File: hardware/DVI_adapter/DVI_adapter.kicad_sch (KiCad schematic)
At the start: 49 parts, among them J1 DF12NB(3.0)-30DS-0.5V(51), J2 DF12NB(3.0)-30DS-0.5V(51), J3 FPC Cable connector 1x20, U2 TFP410, U2 TXS0102DQMR

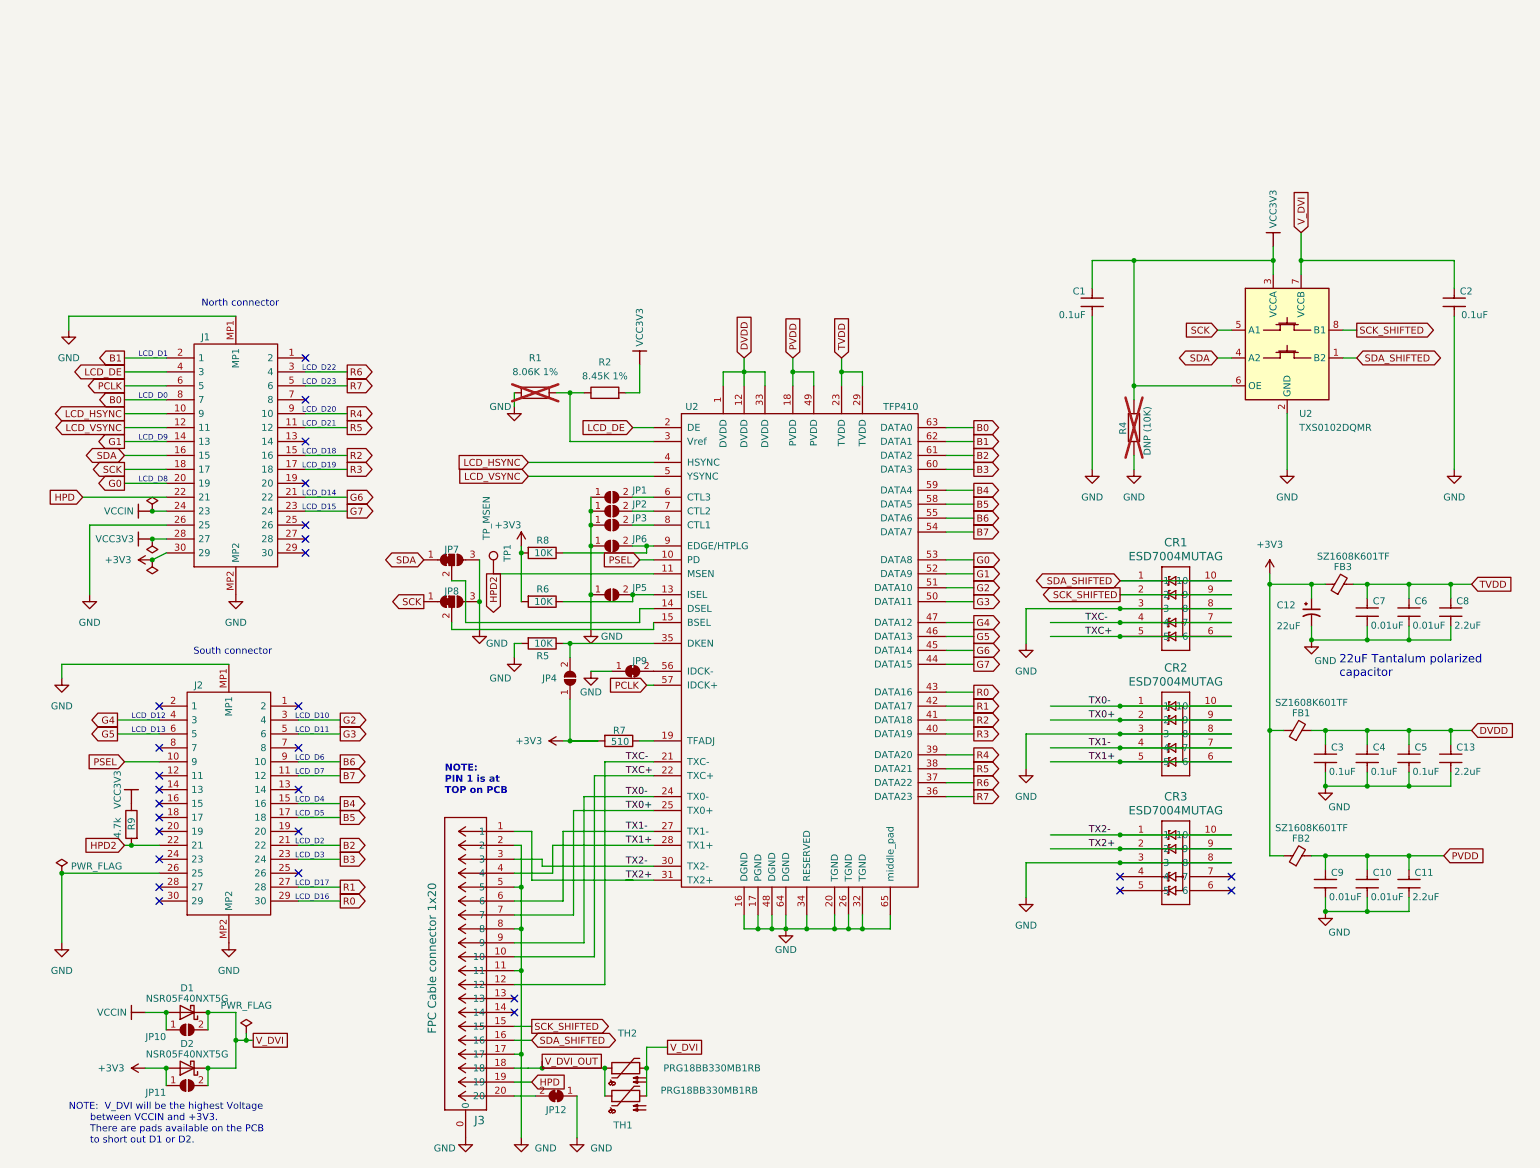
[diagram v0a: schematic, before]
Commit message: Change to 4 layers for better signal integrity. Reorganize differential pins in SSG format to minimize crosstalk at output connector (pinout compatible with common extension cables). Fix level translator footpriont. Add power plane, test points, 5V charge pump, auto reset
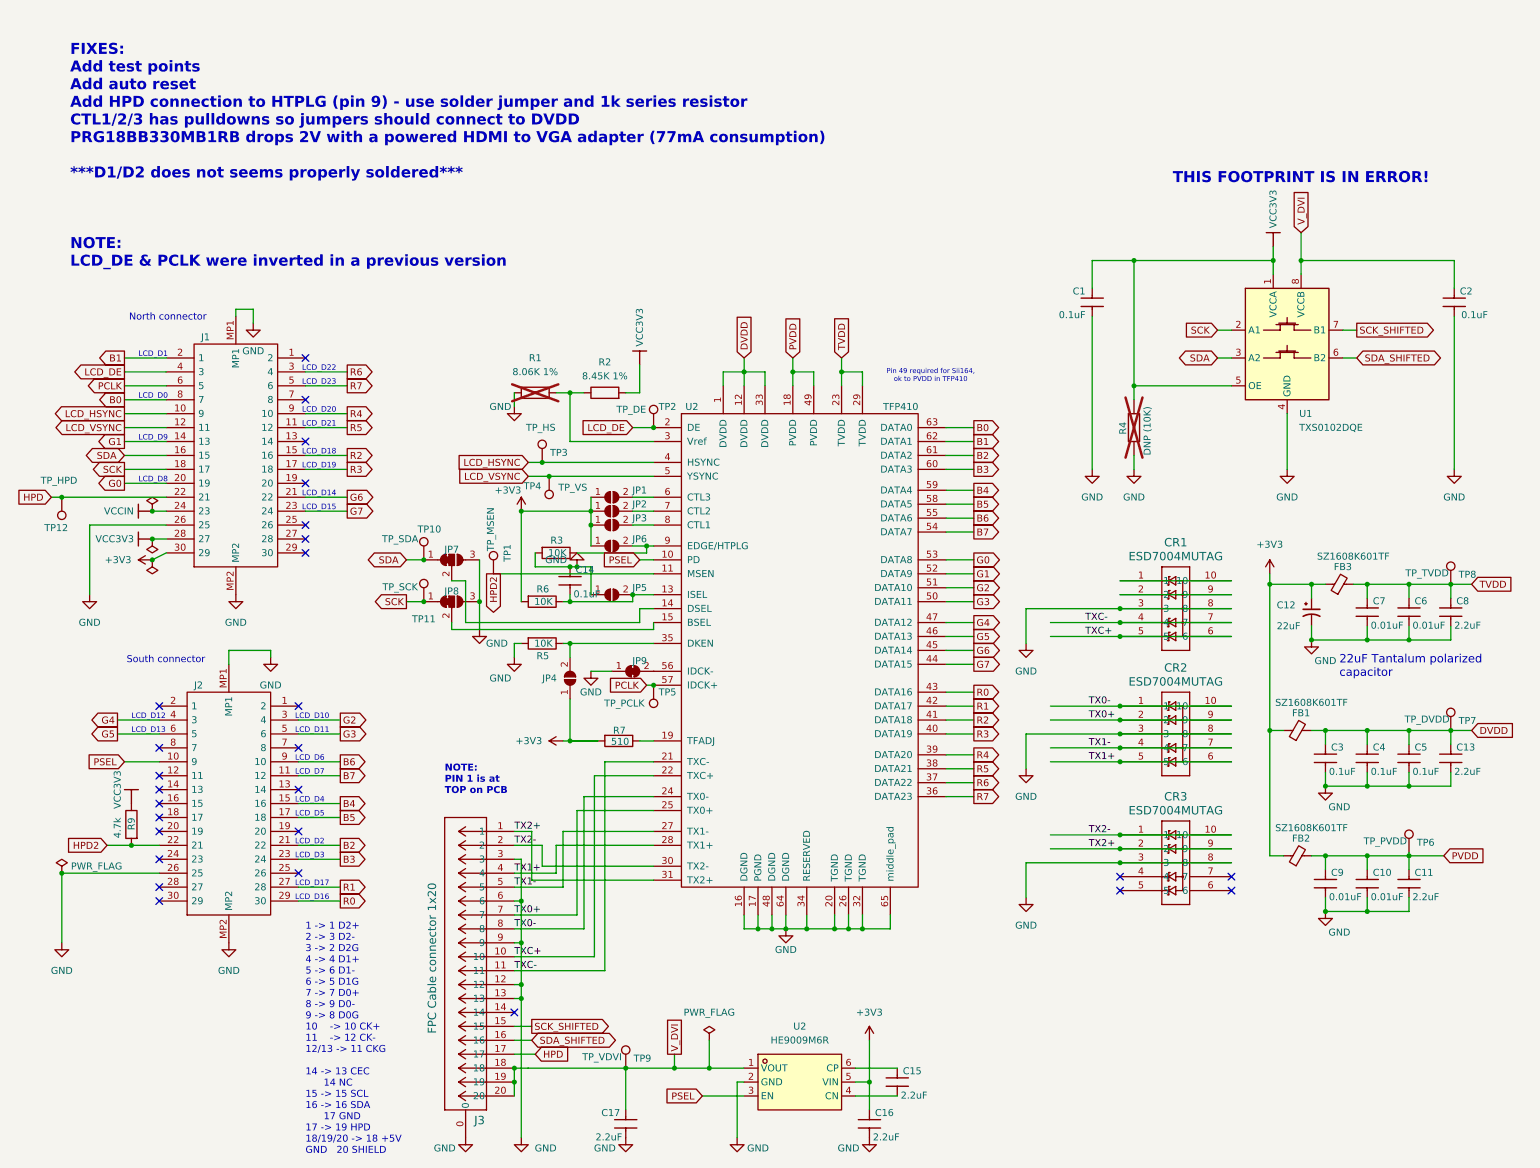
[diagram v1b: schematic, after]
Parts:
- removed D1, D2: NSR05F40NXT5G, Diode_SMD:D_0402_1005Metric, symbol Device:D_Schottky
- removed JP10, JP11: JMP_ISEL, Library:SolderJumper-2_Open_RoundedPad_2.254x0.95mm, symbol Jumper:SolderJumper_2_Open
- removed JP12: JMP_CKn, Library:SolderJumper-2_Closed_RoundedPad_2.254x0.95mm, symbol Jumper:SolderJumper_2_Bridged
- removed R8: 10K, Resistor_SMD:R_0402_1005Metric, symbol Device:R
- removed TH1, TH2: PRG18BB330MB1RB, Fuse:Fuse_0603_1608Metric, symbol Device:Thermistor_PTC
- removed U2: TXS0102DQMR, Library:DQM8, symbol Logic_LevelTranslator:TXS0102DCU
- added C14: 0.1uF, Library:C_0402_1005Metric, symbol Periph-altium-import:0_CAP
- added C15, C16, C17: 2.2uF, Library:C_0402_1005Metric, symbol Periph-altium-import:0_CAP
- added R3: 10K, Resistor_SMD:R_0402_1005Metric, symbol Device:R
- added TP10: TP_SDA, TestPoint:TestPoint_THTPad_1.0x1.0mm_Drill0.5mm, symbol Connector:TestPoint
- added TP11: TP_SCK, TestPoint:TestPoint_THTPad_1.0x1.0mm_Drill0.5mm, symbol Connector:TestPoint
- added TP12: TP_HPD, TestPoint:TestPoint_THTPad_1.0x1.0mm_Drill0.5mm, symbol Connector:TestPoint
- added TP2: TP_DE, TestPoint:TestPoint_Pad_1.5x1.5mm, symbol Connector:TestPoint
- added TP3: TP_HS, TestPoint:TestPoint_Pad_1.5x1.5mm, symbol Connector:TestPoint
- added TP4: TP_VS, TestPoint:TestPoint_Pad_1.5x1.5mm, symbol Connector:TestPoint
- added TP5: TP_PCLK, TestPoint:TestPoint_Pad_1.5x1.5mm, symbol Connector:TestPoint
- added TP6: TP_PVDD, TestPoint:TestPoint_Pad_1.5x1.5mm, symbol Connector:TestPoint
- added TP7: TP_DVDD, TestPoint:TestPoint_THTPad_1.0x1.0mm_Drill0.5mm, symbol Connector:TestPoint
- added TP8: TP_TVDD, TestPoint:TestPoint_Pad_1.5x1.5mm, symbol Connector:TestPoint
- added TP9: TP_VDVI, TestPoint:TestPoint_THTPad_1.0x1.0mm_Drill0.5mm, symbol Connector:TestPoint
- added U1: TXS0102DQE, Package_SON:X2SON-8_1.4x1mm_P0.35mm, symbol Logic_LevelTranslator:TXS0102DQE
- added U2: HE9009M6R, easyeda2kicad:SOT-23-6_L2.9-W1.7-P0.95-LS2.8-BL, symbol easyeda2kicad:HE9009M6R
- J2: footprint DF12NB3030DP05V51 -> Library:DF12NB3030DP05V51; LCSC Part Number (none) -> C2904115; Manufacturer_Part_Number (none) -> DF12NB(3.0)-30DP-0.5V(51)
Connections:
- net V_DVI_OUT is gone; now on net V_DVI: J3.18
- net +3V3: now also JP1.1 (A), JP2.1 (A), JP3.1 (A), JP6.1 (A), C16.1, U2.5 (VIN)
- net DVDD: now also TP7.1
- net GND: now also J3.12, J3.13, J3.3, J3.6, J3.9, C14.1, C16.2, C17.2, R3.2, U1.4 (GND), U2.2 (GND); no longer J3.11, J3.17, J3.2, J3.5, J3.8, JP1.1 (A), JP2.1 (A), JP3.1 (A), JP6.1 (A)
- net HPD: now also J3.17, TP12.1; no longer J3.19
- net LCD_DE: now also TP2.1
- net LCD_HSYNC: now also TP3.1
- net LCD_VSYNC: now also TP4.1
- net PCLK: now also TP5.1
- net PSEL: now also U2.3 (EN)
- net PVDD: now also TP6.1
- net SCK: now also TP11.1, U1.2 (A1)
- net SCK_SHIFTED: now also U1.7 (B1); no longer CR1.2, CR1.9
- net SDA: now also TP10.1, U1.3 (A2)
- net SDA_SHIFTED: now also U1.6 (B2); no longer CR1.1, CR1.10
- net TVDD: now also TP8.1
- net TX0-: now also J3.8; no longer J3.9
- net TX1-: now also J3.5; no longer J3.6
- net TX2-: now also J3.2; no longer J3.3
- net TXC-: now also J3.11; no longer J3.12
- net VCC3V3: now also U1.1 (VCCA), U1.5 (OE)
- net V_DVI: now also J3.19, J3.20, C17.1, TP9.1, U1.8 (VCCB), U2.1 (VOUT)
- net at JP5.2 (B), R6.1, U2.13 (ISEL): now also C14.2
- net at JP6.2 (B), U2.9 (EDGE/HTPLG): now also R3.1
- new net: C15.2, U2.4 (CN)
- new net: C15.1, U2.6 (CP)
- new net: CR1.1, CR1.10
- new net: CR1.2, CR1.9
- no-connect marks 28 -> 27
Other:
- note added: "1 -> 1 D2+ 2 -> 3 D2- 3 -> 2 D2G 4 -> 4 D1+ 5 -> 6 D1- 6 -> 5 D1G 7 -> 7 D0+ 8 -> 9 D0- 9 -> 8 D0G 10 -> 10 CK+ 11 -> 12 CK- 12/13 -> 11 CKG 14 -> 13 CEC 14 NC 15 -> 15 SCL 16 -> 16 SDA 17 GND 17 -> 19 HPD 18/19/20 -> 18 +5V GND 20 SHIELD"
- note added: "FIXES: Add test points Add auto reset Add HPD connection to HTPLG (pin 9) - use solder jumper and 1k series resistor CTL1/2/3 has pulldowns so jumpers should connect to DVDD PRG18BB330MB1RB drops 2V with a powered HDMI to VGA adapter (77mA consumption) ***D1/D2 does not seems properly soldered*** NOTE: LCD_DE & PCLK were inverted in a previous version"
- note added: "Pin 49 required for Sii164, ok to PVDD in TFP410"
- note added: "THIS FOOTPRINT IS IN ERROR!"
- note removed: "NOTE: V_DVI will be the highest Voltage between VCCIN and +3V3. There are pads available on the PCB to short out D1 or D2."

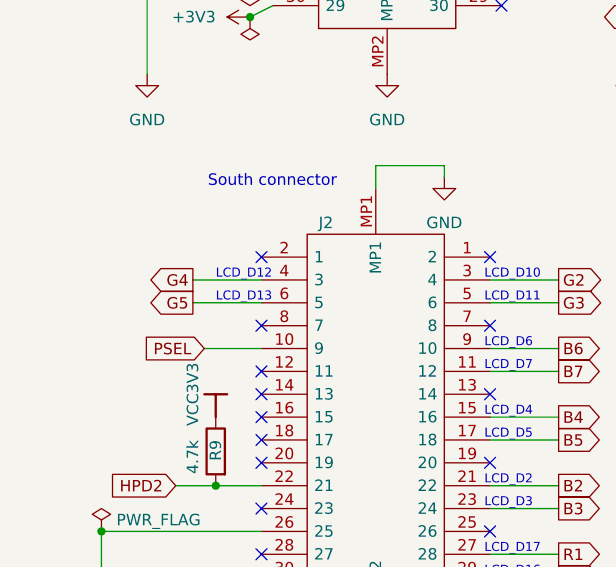
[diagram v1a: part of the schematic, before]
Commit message: fixed mixup of pins G5/G4 (3rd diff pair ODD) and DE/PCLK (3rd diff pair EVEN), now with correct polarity for diff pairs
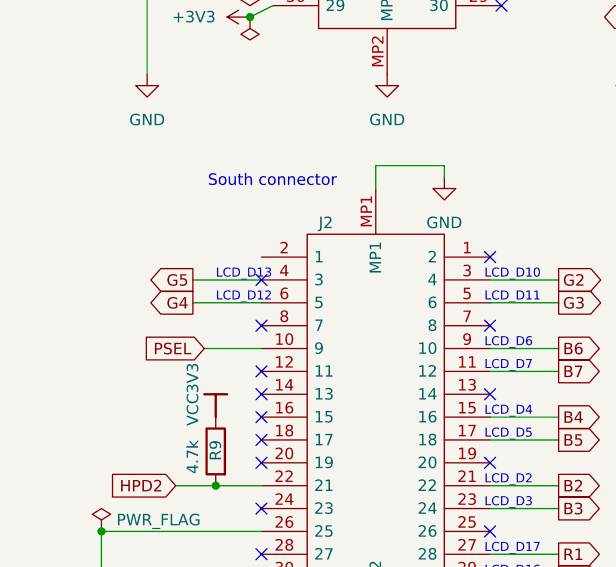
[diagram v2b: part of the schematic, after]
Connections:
- net G4: now also J2.6 (5); no longer J2.4 (3)
- net G5: now also J2.4 (3); no longer J2.6 (5)
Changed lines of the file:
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@@
 	)
 	(no_connect
+		(at 35.56 116.84)
+	)
+	(no_connect
 		(at 62.23 81.28)
 	)
@@
 	)
 	(no_connect
-		(at 35.56 114.3)
-	)
-	(no_connect
 		(at 35.56 132.08)
 	)
@@
 	(wire
 		(pts
-			(xy 27.94 119.38) (xy 35.56 119.38)
-		)
-		(stroke
-			(width 0.254)
-			(type default)
-		)
-	)
-	(wire
-		(pts
 			(xy 35.56 144.78) (xy 17.78 144.78)
 		)
@@
 	(wire
 		(pts
+			(xy 27.94 116.84) (xy 35.56 116.84)
+		)
+		(stroke
+			(width 0.254)
+			(type default)
+		)
+	)
+	(wire
+		(pts
 			(xy 198.12 116.84) (xy 210.82 116.84)
 		)
@@
 	(wire
 		(pts
+			(xy 27.94 119.38) (xy 35.56 119.38)
+		)
+		(stroke
+			(width 0.254)
+			(type default)
+		)
+	)
+	(wire
+		(pts
 			(xy 69.85 78.74) (xy 62.23 78.74)
 		)
@@
 	(wire
 		(pts
-			(xy 27.94 116.84) (xy 35.56 116.84)
-		)
-		(stroke
-			(width 0.254)
-			(type default)
-		)
-	)
-	(wire
-		(pts
 			(xy 110.49 95.25) (xy 121.92 95.25)
 		)
@@
 		)
 	)
+	(text "LCD_D13"
+		(exclude_from_sim no)
+		(at 30.48 116.84 0)
+		(effects
+			(font
+				(size 1 1)
+			)
+			(justify left bottom)
+		)
+	)
 	(text "LCD_D9"
 		(exclude_from_sim no)
@@
 		)
 	)
-	(text "LCD_D13"
+	(text "LCD_D4"
 		(exclude_from_sim no)
-		(at 30.48 119.38 0)
+		(at 60.325 132.08 0)
 		(effects
 			(font
@@
 	(text "LCD_D12"
 		(exclude_from_sim no)
-		(at 30.48 116.84 0)
-		(effects
-			(font
-				(size 1 1)
-			)
-			(justify left bottom)
-		)
-	)
-	(text "LCD_D4"
-		(exclude_from_sim no)
-		(at 60.325 132.08 0)
+		(at 30.48 119.38 0)
 		(effects
 			(font
@@
 		)
 	)
-	(global_label "G4"
-		(shape output)
-		(at 27.94 116.84 180)
-		(fields_autoplaced yes)
-		(effects
-			(font
-				(size 1.27 1.27)
-			)
-			(justify right)
-		)
-		(property "Intersheetrefs" "${INTERSHEET_REFS}"
-			(at 22.4753 116.84 0)
-			(effects
-				(font
-					(size 1.27 1.27)
-				)
-				(justify right)
-				(hide yes)
-			)
-		)
-	)
 	(global_label "TVDD"
 		(shape input)
@@
 		)
 	)
+	(global_label "G4"
+		(shape output)
+		(at 27.94 119.38 180)
+		(fields_autoplaced yes)
+		(effects
+			(font
+				(size 1.27 1.27)
+			)
+			(justify right)
+		)
+		(property "Intersheetrefs" "${INTERSHEET_REFS}"
+			(at 22.4753 119.38 0)
+			(effects
+				(font
+					(size 1.27 1.27)
+				)
+				(justify right)
+				(hide yes)
+			)
+		)
+	)
 	(global_label "DVDD"
 		(shape input)
@@
 		)
 	)
-	(global_label "G5"
-		(shape output)
-		(at 27.94 119.38 180)
-		(fields_autoplaced yes)
-		(effects
-			(font
-				(size 1.27 1.27)
-			)
-			(justify right)
-		)
-		(property "Intersheetrefs" "${INTERSHEET_REFS}"
-			(at 22.4753 119.38 0)
-			(effects
-				(font
-					(size 1.27 1.27)
-				)
-				(justify right)
-				(hide yes)
-			)
-		)
-	)
 	(global_label "R3"
 		(shape output)
@@
 			(effects
 				(font
+					(size 1.27 1.27)
+				)
+				(justify right)
+				(hide yes)
+			)
+		)
+	)
+	(global_label "G5"
+		(shape output)
+		(at 27.94 116.84 180)
+		(fields_autoplaced yes)
+		(effects
+			(font
+				(size 1.27 1.27)
+			)
+			(justify right)
+		)
+		(property "Intersheetrefs" "${INTERSHEET_REFS}"
+			(at 22.4753 116.84 0)
+			(effects
+				(font

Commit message: change 20-pin FPC connector and update part numbers for manufacturing
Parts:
- J3: footprint Library:XFCN_F0501-B-20-20T-R -> easyeda2kicad:FPC-SMD_XUNPU_FPC-0.5FX-20PWBH15; LCSC Part Number C5291557 -> C3446031; MPN (none) -> FPC-0.5FX-20PWBH15
- U1: MPN (none) -> TXS0102DQER
- U2: LCSC Part Number (none) -> C7498519; MPN (none) -> TFP410PAPR
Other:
- note added: "Note other packages has different footprint"
- note removed: "THIS FOOTPRINT IS IN ERROR!"
- company: Copyright (C) 2023-2024 Victor Suarez Rovere -> Copyright (C) 2023-2025 Victor Suarez Rovere
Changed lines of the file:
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@@
 	(title_block
 		(title "DVI Adapter board")
-		(date "2024-05-13")
-		(rev "V0.09")
-		(company "Copyright (C) 2023-2024 Victor Suarez Rovere")
-		(comment 1 "License:  CERN OHL-S")
-		(comment 2 "PCB design:  Mitch Altman &  Victor Suarez Rovere")
-		(comment 3 "Schematics capture:  Mitch Altman & Victor Suarez Rovere")
-		(comment 4 "Circuit design & parts selection:  Victor Suarez Rovere")
+		(date "2026-09-18")
+		(rev "V0.1")
+		(company "Copyright (C) 2023-2025 Victor Suarez Rovere")
 	)
 	(junction
@@
 		)
 	)
-	(text "THIS FOOTPRINT IS IN ERROR!"
+	(text "Note other packages has different footprint"
 		(exclude_from_sim no)
 		(at 243.84 18.034 0)
@@
 			)
 		)
+		(property "MPN" "TXS0102DQER"
+			(at 241.3 48.26 0)
+			(effects
+				(font
+					(size 1.27 1.27)
+				)
+				(hide yes)
+			)
+		)
 		(pin "7"
 		)
@@
 			)
 		)
+		(property "MPN" "TFP410PAPR"
+			(at 130.81 60.96 0)
+			(effects
+				(font
+					(size 1.27 1.27)
+				)
+				(hide yes)
+			)
+		)
+		(property "LCSC Part Number" "C7498519"
+			(at 130.81 60.96 0)
+			(effects
+				(font
+					(size 1.27 1.27)
+				)
+				(hide yes)
+			)
+		)
 		(pin "1"
 		)
@@
 			)
 		)
-		(property "Footprint" "Library:XFCN_F0501-B-20-20T-R"
+		(property "Footprint" "easyeda2kicad:FPC-SMD_XUNPU_FPC-0.5FX-20PWBH15"
 			(at 100.33 185.42 0)
 			(effects
@@
 			)
 		)
-		(property "Datasheet" "https://datasheet.lcsc.com/lcsc/2304140030_XFCN-F0501-B-20-20T-R_C481232.pdf"
+		(property "Datasheet" ""
 			(at 100.33 185.42 0)
 			(effects
@@
 			)
 		)
-		(property "LCSC Part Number" "C5291557"
+		(property "MPN" "FPC-0.5FX-20PWBH15"
+			(at 100.33 185.42 0)
+			(effects
+				(font
+					(size 1.27 1.27)
+				)
+				(hide yes)
+			)
+		)
+		(property "LCSC Part Number" "C3446031"
 			(at 100.33 185.42 0)
 			(effects
